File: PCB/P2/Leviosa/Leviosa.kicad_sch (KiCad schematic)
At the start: 54 parts, among them J1 Barrel_Jack, J2 2.54mm 1x03 Spare, U1 MX27524S

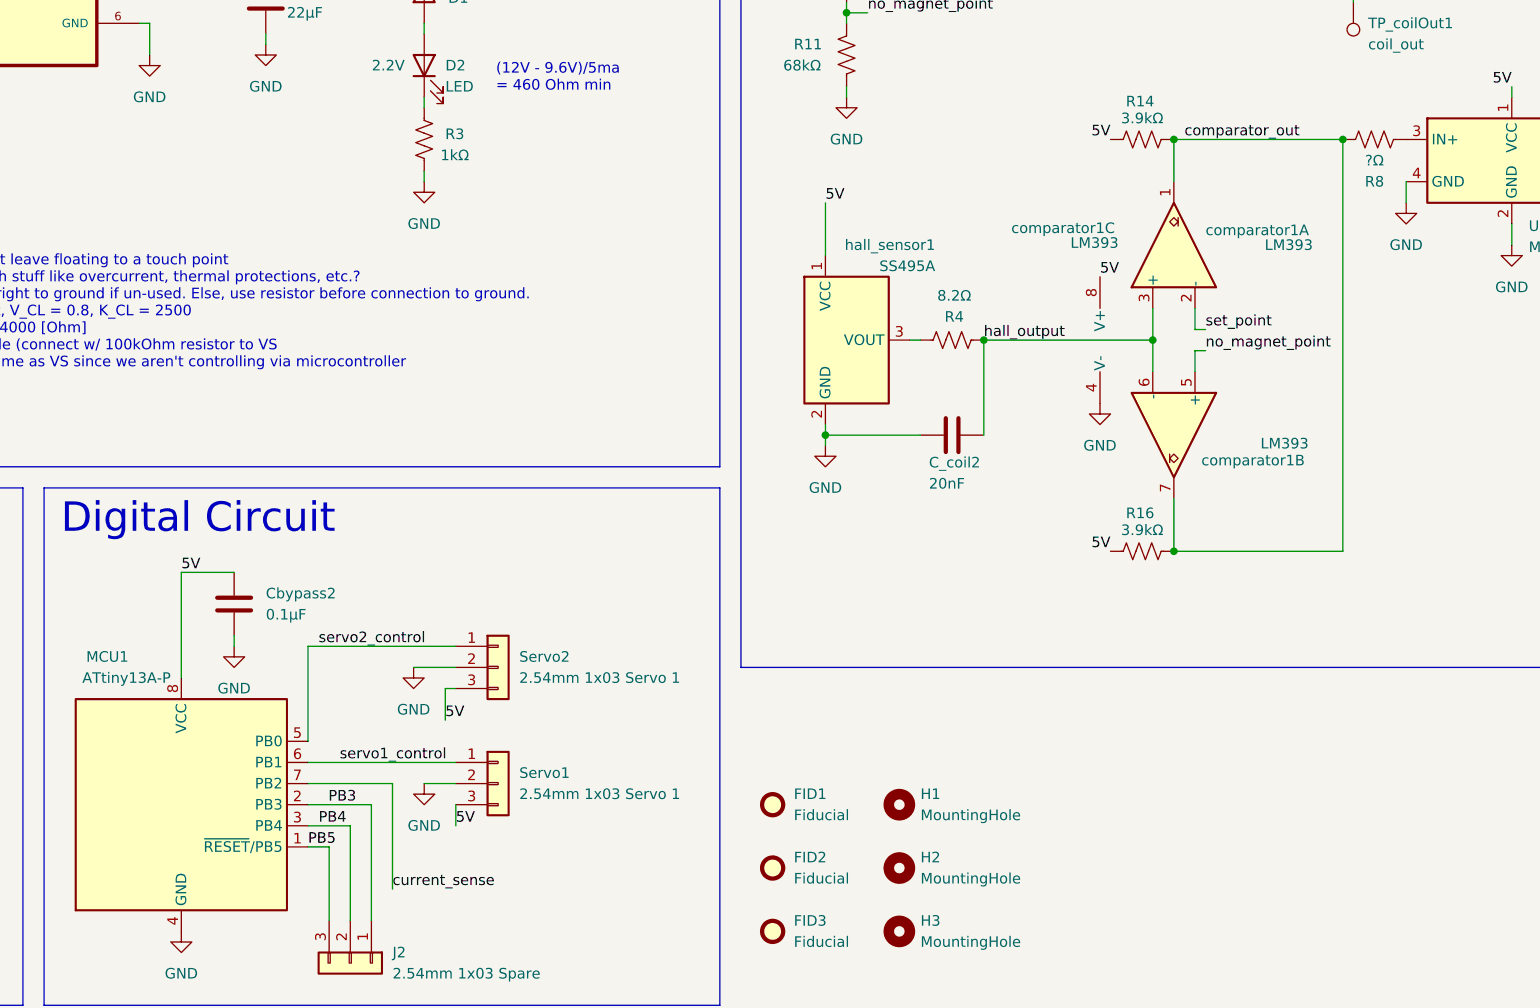
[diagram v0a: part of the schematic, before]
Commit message: update circuit with 0R on comparator output & servo pinout
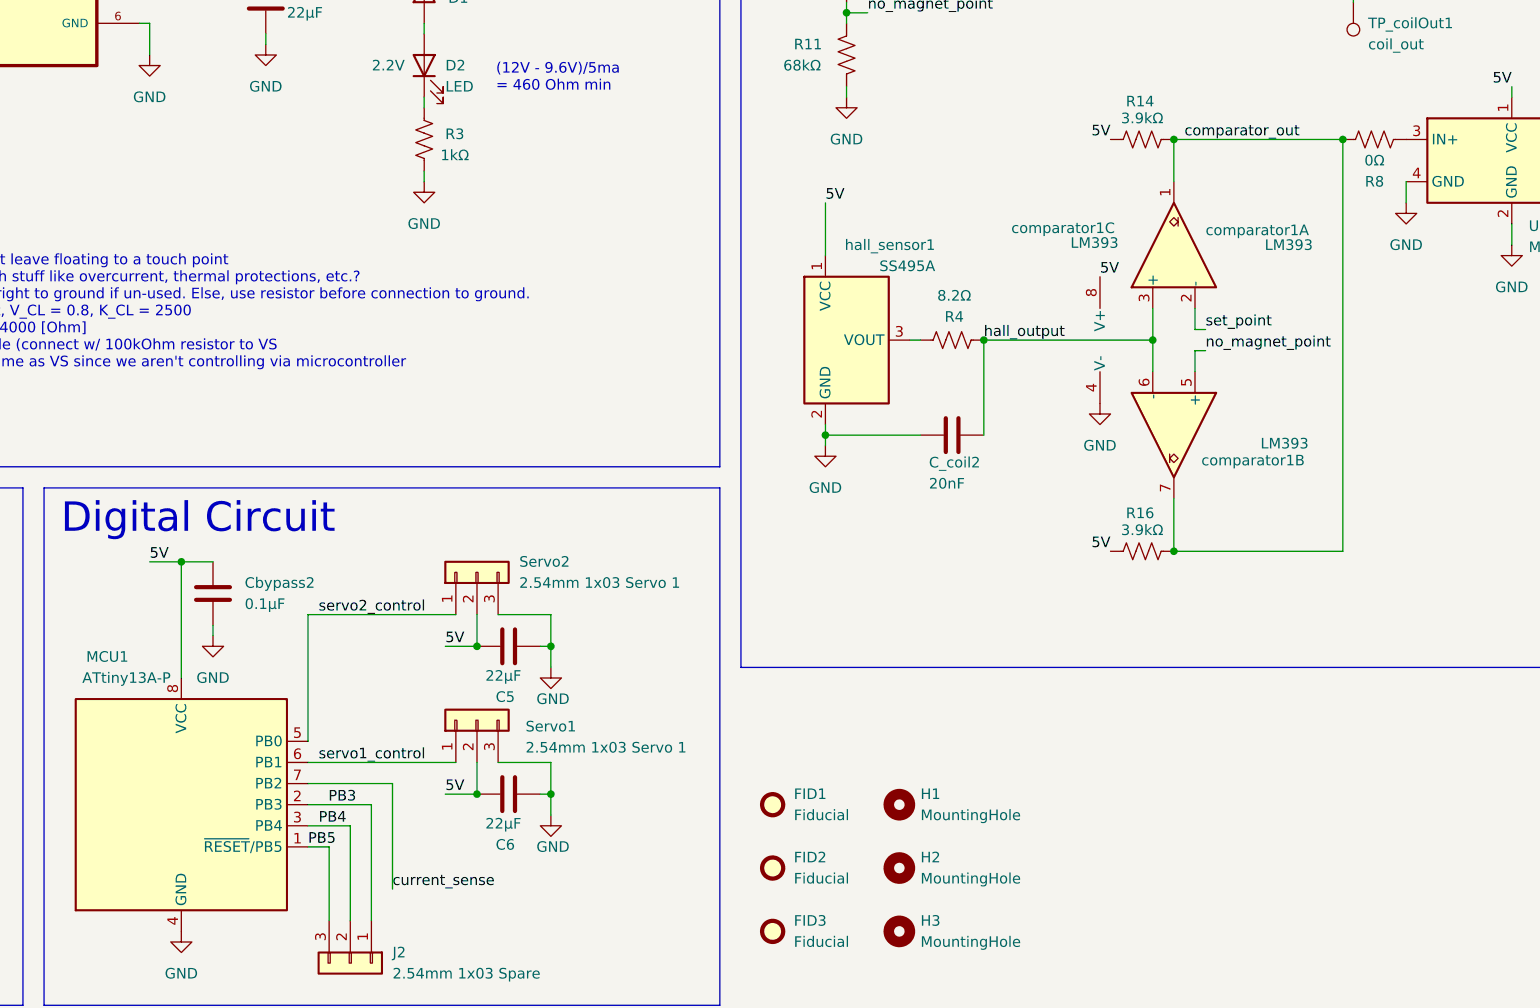
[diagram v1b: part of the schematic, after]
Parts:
- added C5, C6: 22µF, Capacitor_SMD:C_0805_2012Metric, symbol Device:C
- R8: value ?Ω -> 0Ω
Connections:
- net 5V: now also Servo1.2 (Pin_2), Servo2.2 (Pin_2), C5.1, C6.1; no longer Servo1.3 (Pin_3), Servo2.3 (Pin_3)
- net GND: now also Servo1.3 (Pin_3), Servo2.3 (Pin_3), C5.2, C6.2; no longer Servo1.2 (Pin_2), Servo2.2 (Pin_2)
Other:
- moved on the sheet: Cbypass2, Servo1, Servo2

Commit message: fix name
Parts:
- C_coil2: value 20nF -> 2.2nF
- R4: value 8.2Ω -> 10Ω
- U1: value MX27524S -> MX27517
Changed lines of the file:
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@@
 			)
 		)
-		(property "Value" "8.2Ω"
+		(property "Value" "10Ω"
 			(at 159.004 110.236 90)
 			(effects
@@
 			)
 		)
-		(property "Value" "MX27524S"
+		(property "Value" "MX27517"
 			(at 228.092 104.394 0)
 			(effects
@@
 			)
 		)
-		(property "Description" "9A (peak) Gate driver, 12V, 3ns delay, SOT-23-6"
+		(property "Description" "-40℃~+125℃ 1 10ns 15ns 4V~18V 6ns 6ns 80uA Low Side MOSFET SOT-23-6L Gate Drivers ROHS"
+			(at 226.06 93.98 0)
+			(effects
+				(font
+					(size 1.27 1.27)
+				)
+				(hide yes)
+			)
+		)
+		(property "Link" ""
 			(at 226.06 93.98 0)
 			(effects
@@
 			)
 		)
-		(property "Value" "20nF"
+		(property "Value" "2.2nF"
 			(at 155.956 132.842 90)
 			(effects

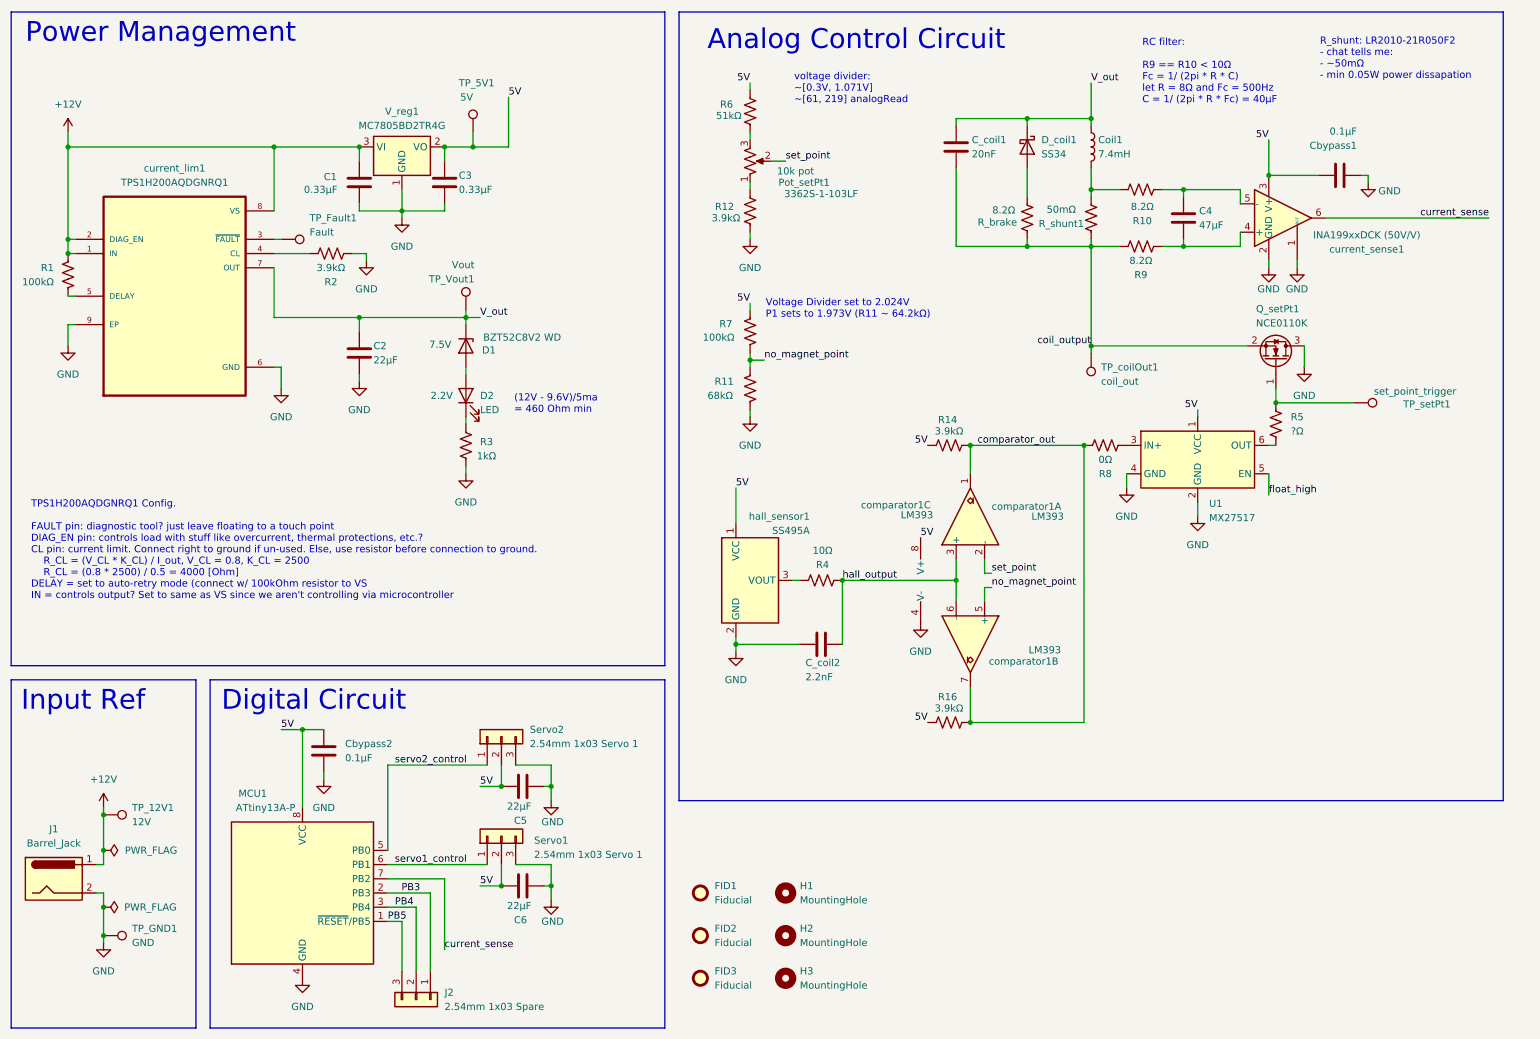
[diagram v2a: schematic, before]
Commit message: add unity buffer op amp
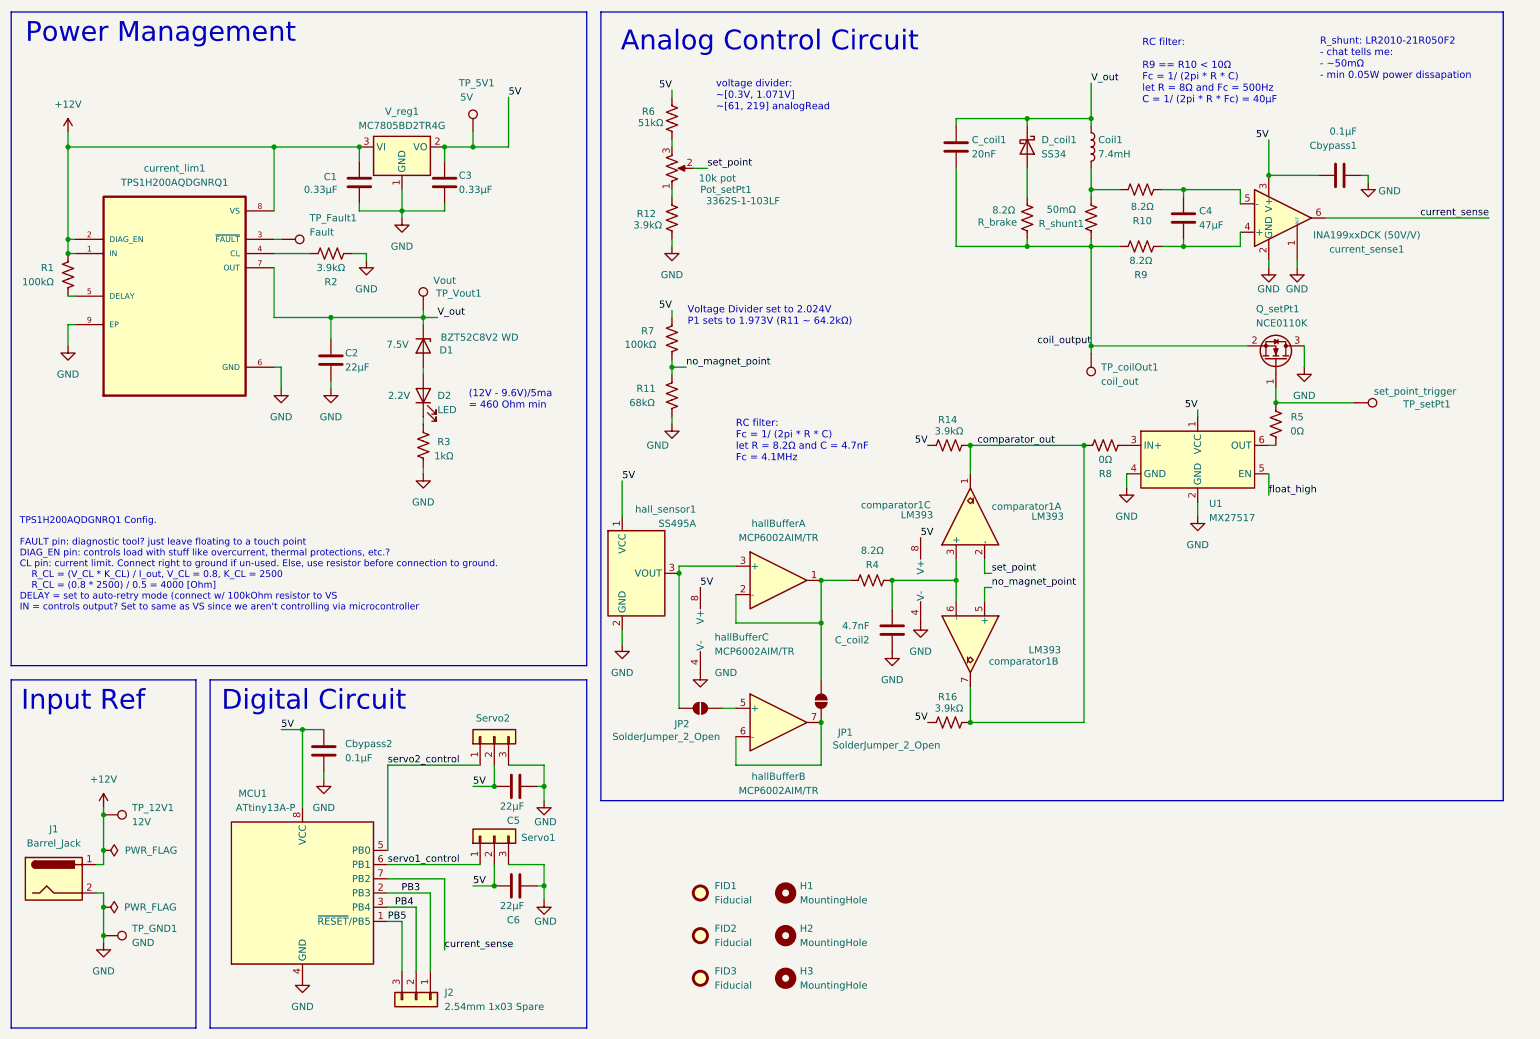
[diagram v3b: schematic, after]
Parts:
- added JP1, JP2: SolderJumper_2_Open, Jumper:SolderJumper-2_P1.3mm_Open_Pad1.0x1.5mm, symbol Jumper:SolderJumper_2_Open
- added hallBuffer: MCP6002AIM/TR, Package_SO:MSOP-8_3x3mm_P0.65mm, symbol Amplifier_Operational:MCP6002-xSN
- C_coil2: value 2.2nF -> 4.7nF; Link https://jlcpcb.com/partdetail/1954-0603B203K500NT/C1602 -> https://jlcpcb.com/partdetail/1890-0402B472K500NT/C1538
- R4: value 10Ω -> 8.2Ω
- R5: value ?Ω -> 0Ω
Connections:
- net 5V: now also hallBuffer.8 (V+)
- net GND: now also C_coil2.1, hallBuffer.4 (V-); no longer C_coil2.2
- net at R4.1: now also JP1.2 (B), hallBuffer.1, hallBuffer.2 (-); no longer hall_sensor1.3 (VOUT)
- net hall_output: no longer names the net of R4.2, comparator1.3 (+), comparator1.6 (-)
- net hall_output: now also C_coil2.2; no longer C_coil2.1
- new net: JP2.2 (B), hallBuffer.5 (+)
- new net: JP1.1 (A), hallBuffer.6 (-), hallBuffer.7
- new net: JP2.1 (A), hallBuffer.3 (+), hall_sensor1.3 (VOUT)
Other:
- note added: "RC filter: Fc = 1/ (2pi * R * C) let R = 8.2Ω and C = 4.7nF Fc = 4.1MHz"
- moved on the sheet: C2, C5, C6, C_coil2, D1, D2, Pot_setPt1, R11, R12, R3, R4, R6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

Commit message: update schematic with single instrumental amplifier (instead of double)
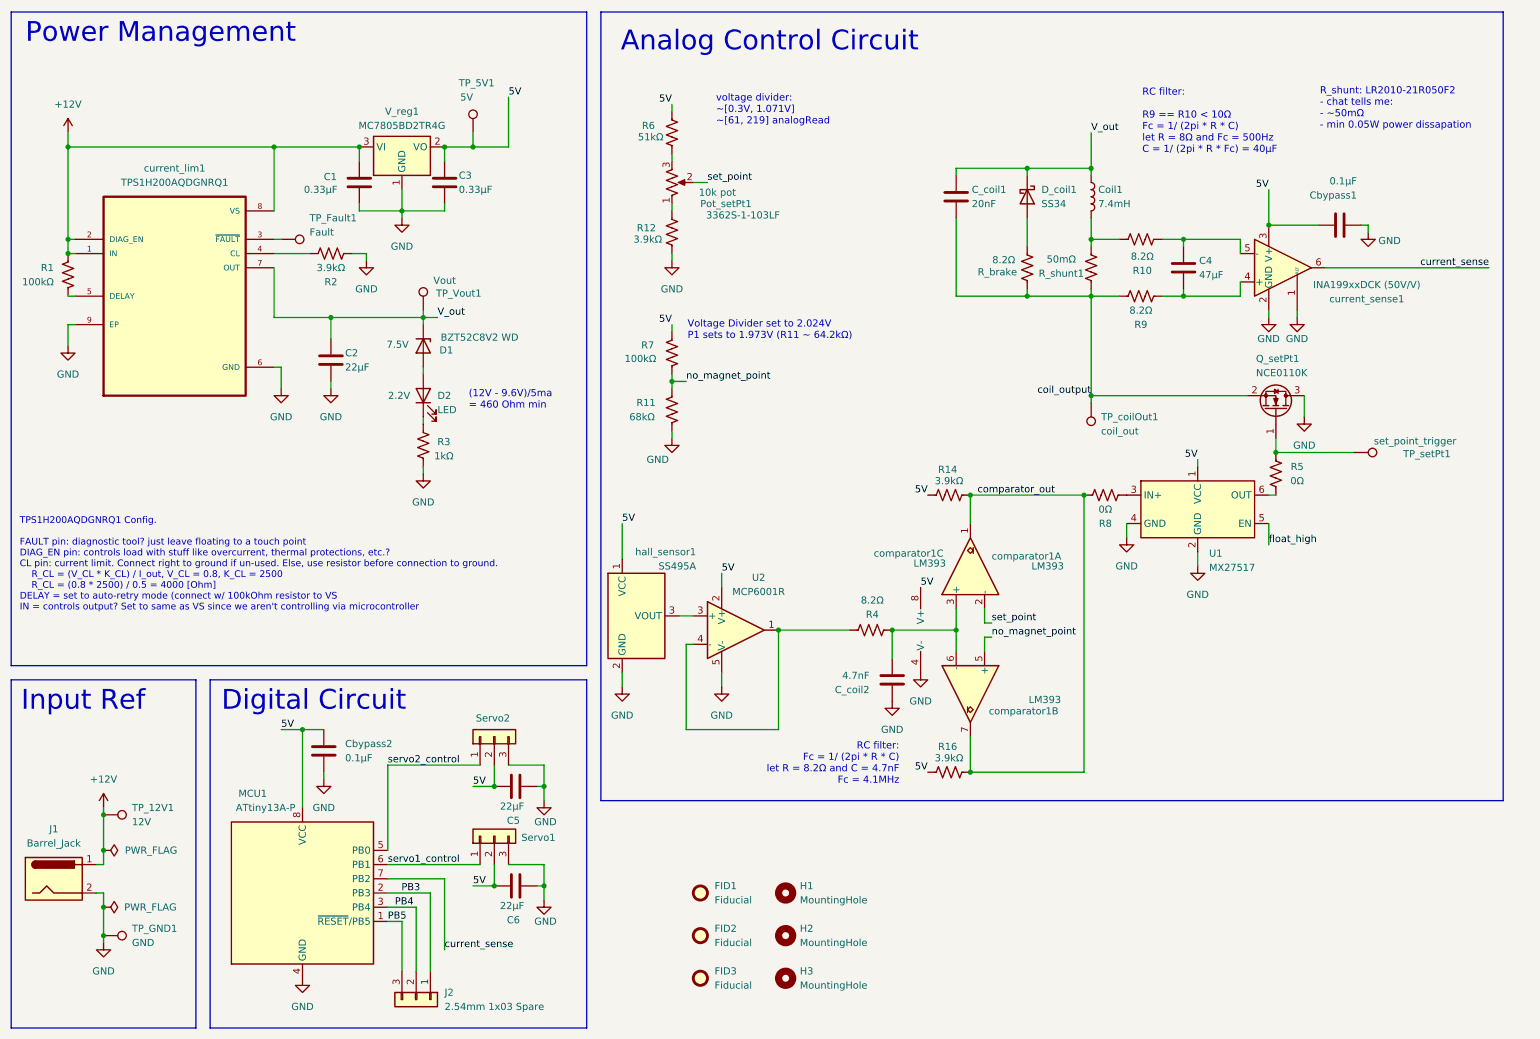
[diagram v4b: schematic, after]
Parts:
- removed JP1, JP2: SolderJumper_2_Open, Jumper:SolderJumper-2_P1.3mm_Open_Pad1.0x1.5mm, symbol Jumper:SolderJumper_2_Open
- removed hallBuffer: MCP6002AIM/TR, Package_SO:MSOP-8_3x3mm_P0.65mm, symbol Amplifier_Operational:MCP6002-xSN
- added U2: MCP6001R, Package_TO_SOT_SMD:SOT-23-5, symbol Amplifier_Operational:MCP6001R
- comparator1: footprint Package_SO:SOIC-8_5.3x5.3mm_P1.27mm -> Package_SO:SOIC-8_3.9x4.9mm_P1.27mm; Link (none) -> https://jlcpcb.com/partdetail/onsemi-LM393DR2G/C7955
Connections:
- net 5V: now also U2.2 (V+)
- net GND: now also U2.5 (V-)
- net at R4.1: now also U2.1, U2.4 (-)
- net at hall_sensor1.3 (VOUT): now also U2.3 (+)
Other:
- moved on the sheet: C4, C_coil1, C_coil2, Cbypass1, Coil1, D_coil1, Pot_setPt1, Q_setPt1, R10, R11, R12, R14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

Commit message: fix naming of folders
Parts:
- removed C5, C6: 22µF, Capacitor_SMD:C_0805_2012Metric, symbol Device:C
- removed C_coil2: 4.7nF, Capacitor_SMD:C_0805_2012Metric_Pad1.18x1.45mm_HandSolder, symbol Device:C
- removed R_brake: 8.2Ω, Resistor_SMD:R_1206_3216Metric, symbol Device:R_US
- removed U1: MX27517, Package_TO_SOT_SMD:SOT-23-6, symbol Driver_FET:ZXGD3001E6
- removed U2: MCP6001R, Package_TO_SOT_SMD:SOT-23-5, symbol Amplifier_Operational:MCP6001R
- added 0R1: DNP, Resistor_SMD:R_0603_1608Metric, symbol Device:R_US
- added Q_noMag1: NCE0110K, Package_TO_SOT_SMD:TO-252-2, symbol Transistor_FET:DMN61D8LQ
- added R13: 330Ω, Resistor_SMD:R_0805_2012Metric_Pad1.20x1.40mm_HandSolder, symbol Device:R_US
- added R15: 0Ω, Resistor_SMD:R_0603_1608Metric, symbol Device:R_US
- added TP_noMag1: no_magnet_point_trigger, TestPoint:TestPoint_Pad_D1.5mm, symbol Connector:TestPoint
- C1, C3: value 0.33µF -> 22µF
- R4: value 8.2Ω -> DNP; footprint Resistor_SMD:R_1206_3216Metric -> Resistor_SMD:R_0603_1608Metric; Link https://jlcpcb.com/partdetail/18710-1206W4F820KT5E/C18022 -> (none); now not fitted
- R5: footprint Resistor_SMD:R_1206_3216Metric -> Resistor_SMD:R_0603_1608Metric; Link https://jlcpcb.com/partdetail/18710-1206W4F820KT5E/C18022 -> (none)
- R8: value 0Ω -> 330Ω; footprint Resistor_SMD:R_1206_3216Metric -> Resistor_SMD:R_0805_2012Metric_Pad1.20x1.40mm_HandSolder; Link https://jlcpcb.com/partdetail/18710-1206W4F820KT5E/C18022 -> (none)
- V_reg1: value MC7805BD2TR4G -> LM7805; footprint Package_TO_SOT_SMD:TO-263-2 -> Package_TO_SOT_SMD:SOT-223-3_TabPin2
- comparator1: footprint Package_SO:SOIC-8_3.9x4.9mm_P1.27mm -> Package_SO:SOIC-8_5.3x5.3mm_P1.27mm; Link https://jlcpcb.com/partdetail/onsemi-LM393DR2G/C7955 -> (none)
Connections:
- net 5V: now also R4.2, Servo1.3 (Pin_3), Servo2.3 (Pin_3); no longer Servo1.2 (Pin_2), Servo2.2 (Pin_2)
- net GND: now also R5.1, Servo1.2 (Pin_2), Servo2.2 (Pin_2), Q_noMag1.3 (D); no longer Q_setPt1.3 (D), Servo1.3 (Pin_3), Servo2.3 (Pin_3), current_sense1.1 (REF)
- net V_out: now also R9.1, R_shunt1.2; no longer C_coil1.1, Coil1.1, D_coil1.1 (K)
- net coil_output: now also Coil1.2, D_coil1.2 (A), 0R1.2; no longer R9.1, R_shunt1.2
- net at R4.1: now also R5.2, current_sense1.1 (REF)
- net hall_output: now reaches comparator1.3 (+), comparator1.6 (-)
- net hall_output: now also hall_sensor1.3 (VOUT); no longer R4.2
- net set_point_trigger: now reaches R8.2
- net set_point_trigger: now also R14.1, comparator1.1
- net at Q_setPt1.1 (G), TP_setPt1.1: now also R8.1; no longer R5.2
- removed net comparator_out: R14.1, R16.1, R8.1, comparator1.1, comparator1.7
- new net: Q_noMag1.1 (G), R13.1, TP_noMag1.1
- new net: 0R1.1, R10.1, R15.2
- new net: C_coil1.1, Coil1.1, D_coil1.1 (K), R15.1, R_shunt1.1
- new net no_magnet_point_trigger: R13.2, R16.1, comparator1.7
- new net transistor1_output: Q_noMag1.2 (S), Q_setPt1.3 (D)
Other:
- note added: "R7 and R8: - short R8 to ground for base case - put in voltage divider if needed to offset current readings"
- note removed: "RC filter: Fc = 1/ (2pi * R * C) let R = 8.2Ω and C = 4.7nF Fc = 4.1MHz"
- moved on the sheet: C2, C4, C_coil1, Cbypass1, Cbypass2, Coil1, D1, D2, D_coil1, Pot_setPt1, Q_setPt1, R10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
